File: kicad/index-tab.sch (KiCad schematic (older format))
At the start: 39 parts, among them J1 USB_C_Receptacle_USB2.0, SW1 SW_Push, U1 ATmega32U4-AU, Y1 16MHz

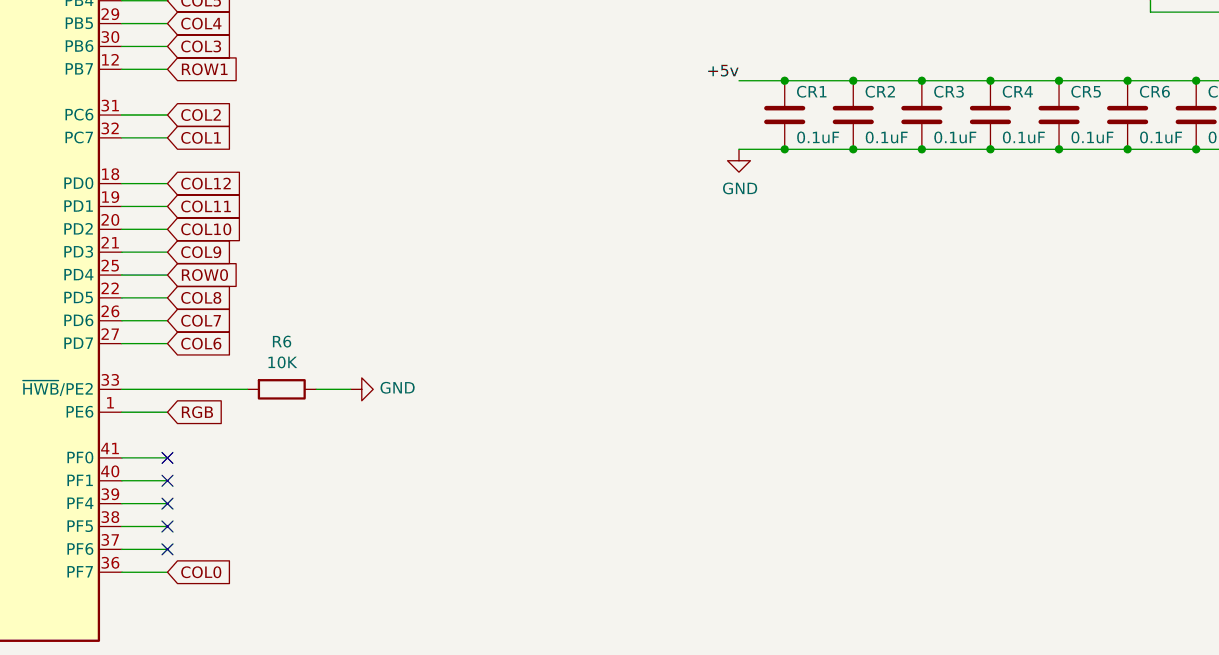
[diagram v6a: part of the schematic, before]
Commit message: OLED screen added
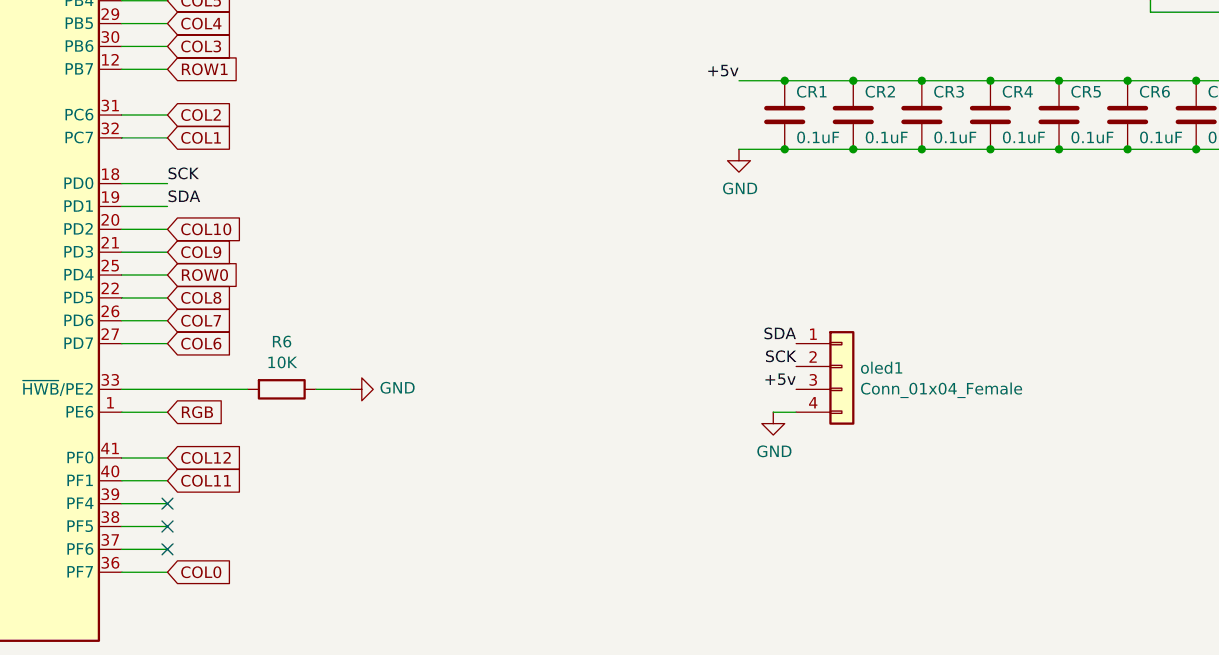
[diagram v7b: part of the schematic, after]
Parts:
- added oled1: Conn_01x04_Female, Connector_PinSocket_2.00mm:PinSocket_1x04_P2.00mm_Vertical, symbol Connector_Generic:Conn_01x04
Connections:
- net +5v: now also oled1.3 (Pin_3)
- net COL11: now also U1.40 (PF1); no longer U1.19 (PD1)
- net COL12: now also U1.41 (PF0); no longer U1.18 (PD0)
- net GND: now also oled1.4 (Pin_4)
- new net SCK: U1.18 (PD0), oled1.2 (Pin_2)
- new net SDA: U1.19 (PD1), oled1.1 (Pin_1)
- no-connect marks 8 -> 6
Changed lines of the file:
@@
 NoConn ~ 1800 3900
 NoConn ~ 1800 4000
-Text GLabel 5300 4050 2    50   Input ~ 0
+Text GLabel 5300 5250 2    50   Input ~ 0
 COL11
 Wire Wire Line
@@
 Wire Wire Line
 	5100 5250 5300 5250
-Text GLabel 5300 3950 2    50   Input ~ 0
+Text GLabel 5300 5150 2    50   Input ~ 0
 COL12
 Wire Wire Line
@@
 Wire Wire Line
 	5100 4350 5300 4350
-NoConn ~ 5300 5150
 NoConn ~ 5300 5550
 NoConn ~ 5300 5450
@@
 	1    0    0    -1
 $EndComp
-NoConn ~ 5300 5250
 Text GLabel 5300 5650 2    50   Input ~ 0
 COL0
@@
 	4400 2300 4500 2300
 Connection ~ 4500 2300
+Text Label 5300 3950 0    50   ~ 0
+SCK
+Text Label 5300 4050 0    50   ~ 0
+SDA
+Text Label 8050 4750 2    50   ~ 0
+SCK
+Text Label 8050 4650 2    50   ~ 0
+SDA
+$Comp
+L power:GND #PWR012
+U 1 1 5EE1F120
+P 7950 4950
+F 0 "#PWR012" H 7950 4700 50  0001 C CNN
+F 1 "GND" H 7955 4777 50  0000 C CNN
+F 2 "" H 7950 4950 50  0001 C CNN
+F 3 "" H 7950 4950 50  0001 C CNN
+	1    7950 4950
+	1    0    0    -1
+$EndComp
+Text Label 8050 4850 2    50   ~ 0
++5v
+$Comp
+L Connector_Generic:Conn_01x04 oled1
+U 1 1 5EE2034B
+P 8250 4750
+F 0 "oled1" H 8330 4742 50  0000 L CNN
+F 1 "Conn_01x04_Female" H 8330 4651 50  0000 L CNN
+F 2 "Connector_PinSocket_2.00mm:PinSocket_1x04_P2.00mm_Vertical" H 8250 4750 50  0001 C CNN
+F 3 "~" H 8250 4750 50  0001 C CNN
+	1    8250 4750
+	1    0    0    -1
+$EndComp
+Wire Wire Line
+	7950 4950 8050 4950
 $EndSCHEMATC
